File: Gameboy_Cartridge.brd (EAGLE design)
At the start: 49.3 x 48 mm, 5 parts, among them IC1 AT49F040J

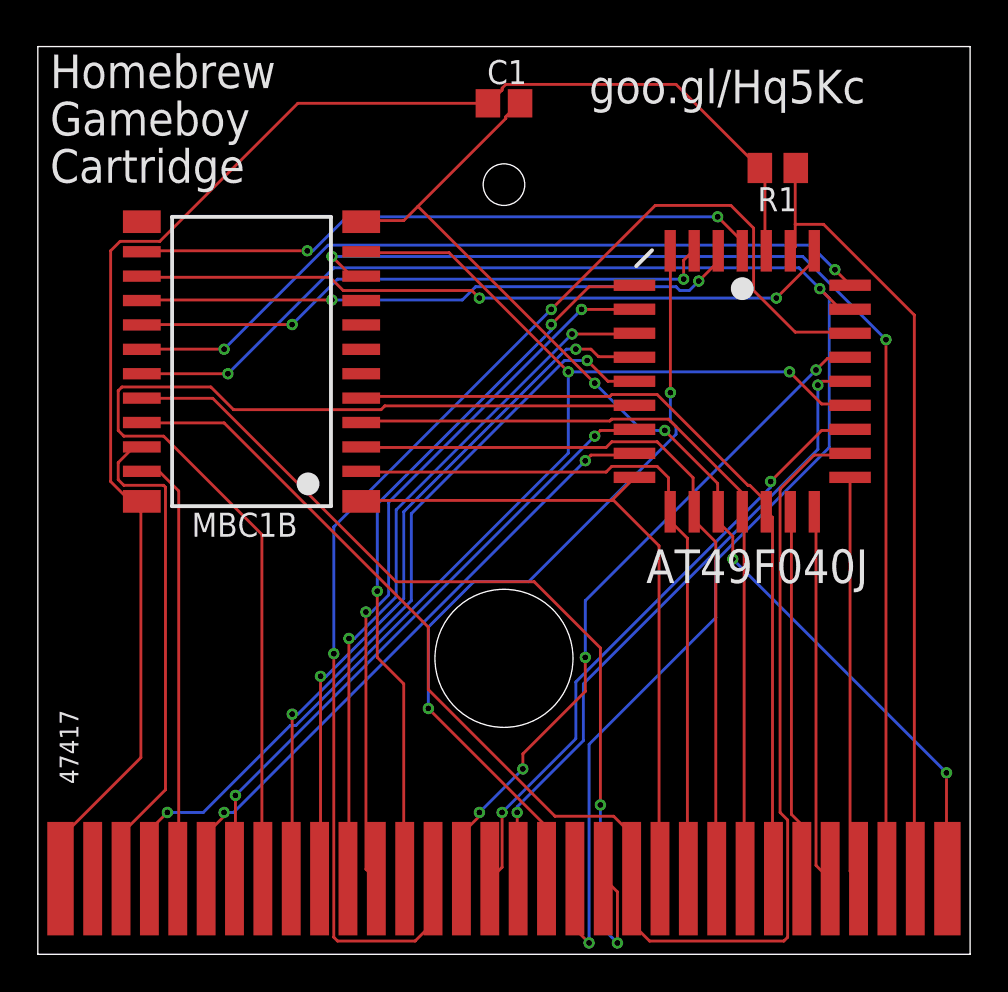
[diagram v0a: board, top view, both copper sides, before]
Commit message: remove old chips and routing
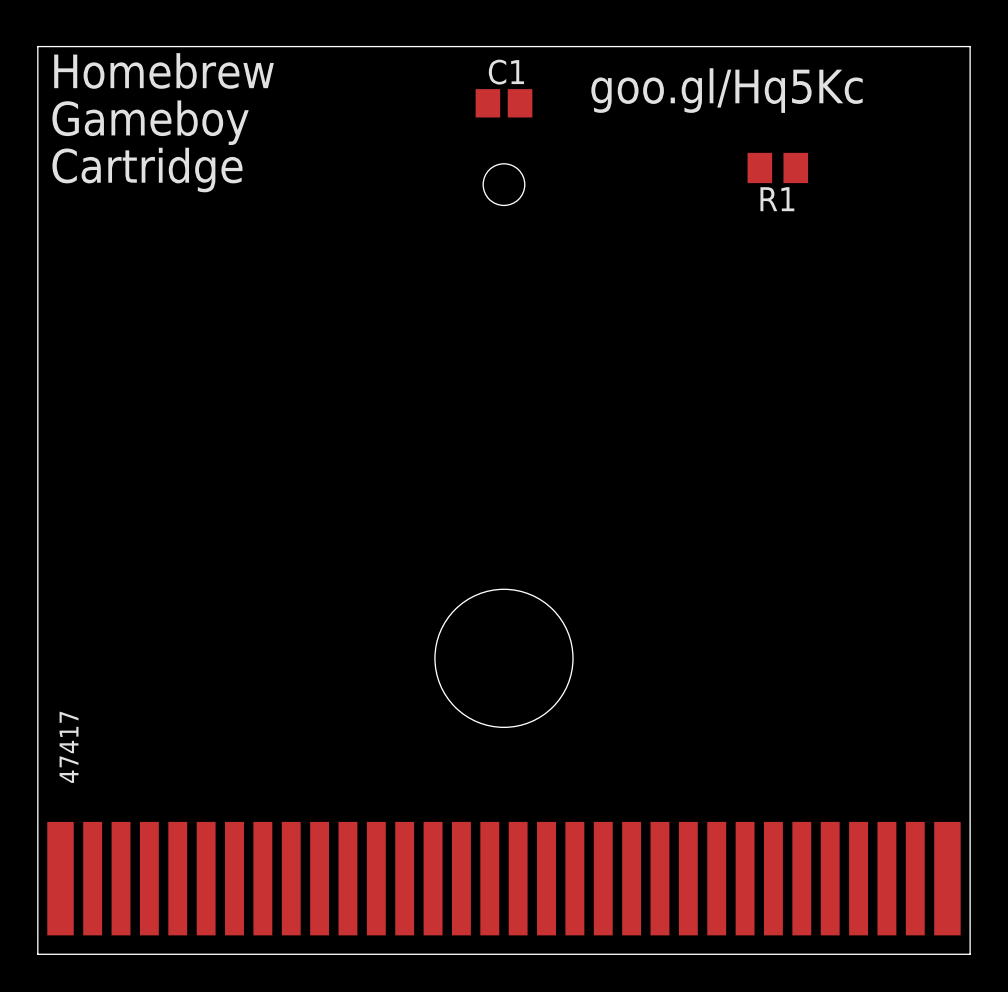
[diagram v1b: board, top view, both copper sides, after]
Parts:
- removed IC1: AT49F040J, gameboy:PLCC32R
- removed U$2: MBC1B, gameboy:MBC1B
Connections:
- removed net 10: IC1.8, U$1.10
- removed net 11: IC1.7, U$1.11
- removed net 12: IC1.6, U$1.12
- removed net 13: IC1.5, U$1.13
- removed net 14: IC1.27, U$1.14
- removed net 15: IC1.26, U$1.15
- removed net 16: IC1.23, U$1.16
- removed net 17: IC1.25, U$1.17
- removed net 18: IC1.4, U$1.18
- removed net 19: IC1.28, U$1.19, U$2.19
- removed net 20: U$1.20, U$2.20
- removed net 21: IC1.22, U$1.21, U$2.21
- removed net 22: IC1.13, U$1.22, U$2.1
- removed net 23: IC1.14, U$1.23, U$2.2
- removed net 24: IC1.15, U$1.24, U$2.3
- removed net 25: IC1.17, U$1.25, U$2.4
- removed net 26: IC1.18, U$1.26, U$2.5
- removed net 27: IC1.19, U$1.27
- removed net 28: IC1.20, U$1.28
- removed net 29: IC1.21, U$1.29
- removed net 3: U$1.3, U$2.22
- removed net 30: U$1.30, U$2.10
- removed net 4: IC1.24, U$1.4, U$2.11
- removed net 5: U$1.5, U$2.23
- removed net 6: IC1.12, U$1.6
- removed net 7: IC1.11, U$1.7
- removed net 8: IC1.10, U$1.8
- removed net 9: IC1.9, U$1.9
- removed net A: IC1.1, U$2.14
- removed net B: IC1.30, U$2.15
- removed net C: IC1.2, U$2.16
- removed net D: IC1.3, U$2.17
- removed net E: IC1.29, U$2.18
- net 31: no longer IC1.31
- net GND: no longer IC1.16, U$2.12
- net VDD: no longer IC1.32, U$2.24
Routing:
- net 19: track 84.5 -> 0.00 mm, vias 3 -> 0
- net VDD: track 81.2 -> 0.00 mm
- net 21: track 78.7 -> 0.00 mm
- net 14: track 68.9 -> 0.00 mm, vias 2 -> 0
- net 4: track 66.5 -> 0.00 mm, vias 3 -> 0
- net 30: track 61.7 -> 0.00 mm, vias 2 -> 0
- net GND: track 59.0 -> 0.00 mm, vias 4 -> 0
- net 8: track 58.2 -> 0.00 mm
- net 20: track 49.4 -> 0.00 mm, vias 2 -> 0
- net 26: track 44.0 -> 0.00 mm
- net 18: track 43.1 -> 0.00 mm, vias 2 -> 0
- net 31: track 42.7 -> 0.00 mm
- net 25: track 42.3 -> 0.00 mm
- net E: track 40.6 -> 0.00 mm, vias 2 -> 0
- net 24: track 40.3 -> 0.00 mm
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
